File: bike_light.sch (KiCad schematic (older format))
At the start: 1 part

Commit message: Minor fixes, labels, etc
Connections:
- wire segments 70 -> 72
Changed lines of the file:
@@
 Sheet 1 18
 Title "Bike Light"
-Date "10 dec 2013"
+Date "11 dec 2013"
 Rev "1.0"
 Comp ""
@@
 F4 "~RESET" I L 7000 1800 60
 F5 "BATT_IN" I L 7000 1150 60
+F6 "PWR_GOOD" O R 7900 1650 60
+F7 "PWR_EN" I L 7000 1250 60
 $EndSheet
 $Sheet
@@
 Wire Wire Line
 	5200 5350 5500 5350
+Wire Wire Line
+	6900 1150 6900 1250
+Wire Wire Line
+	6900 1250 7000 1250
+Connection ~ 6900 1150
 $EndSCHEMATC

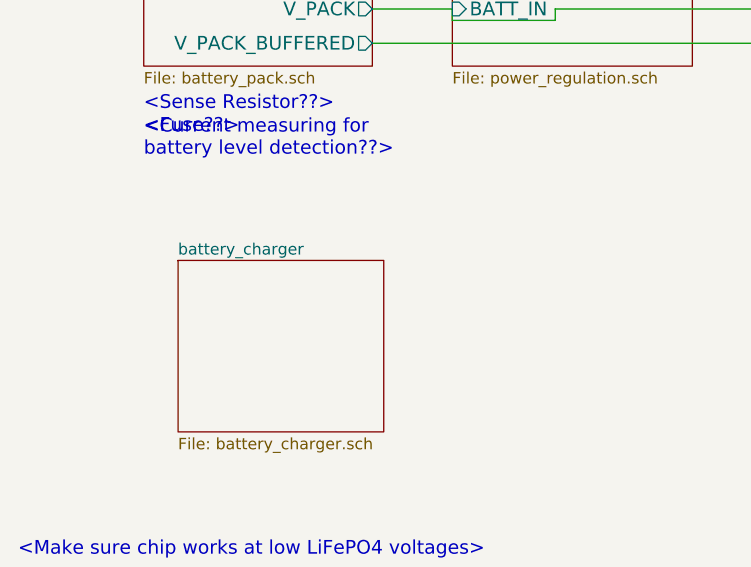
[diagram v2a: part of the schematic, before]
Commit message: started working on charging IC
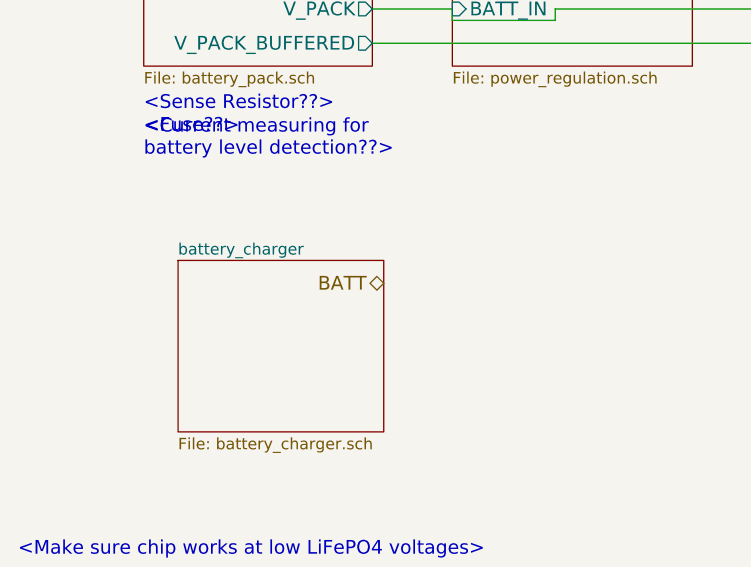
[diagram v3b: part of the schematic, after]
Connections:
- net labels added: BATT
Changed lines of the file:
@@
 Sheet 1 18
 Title "Bike Light"
-Date "11 dec 2013"
+Date "12 dec 2013"
 Rev "1.0"
 Comp ""
@@
 	6900 1250 7000 1250
 Connection ~ 6900 1150
+Text HLabel 2250 2350 0    60   BiDi ~ 0
+BATT
 $EndSCHEMATC

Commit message: uh. same as before? some glitch
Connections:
- wire segments 72 -> 71
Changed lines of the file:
@@
 Sheet 1 18
 Title "Bike Light"
-Date "12 dec 2013"
+Date "13 dec 2013"
 Rev "1.0"
 Comp ""
@@
 $EndSheet
 Wire Wire Line
-	2200 1150 2550 1150
-Wire Wire Line
 	2550 1150 2550 1200

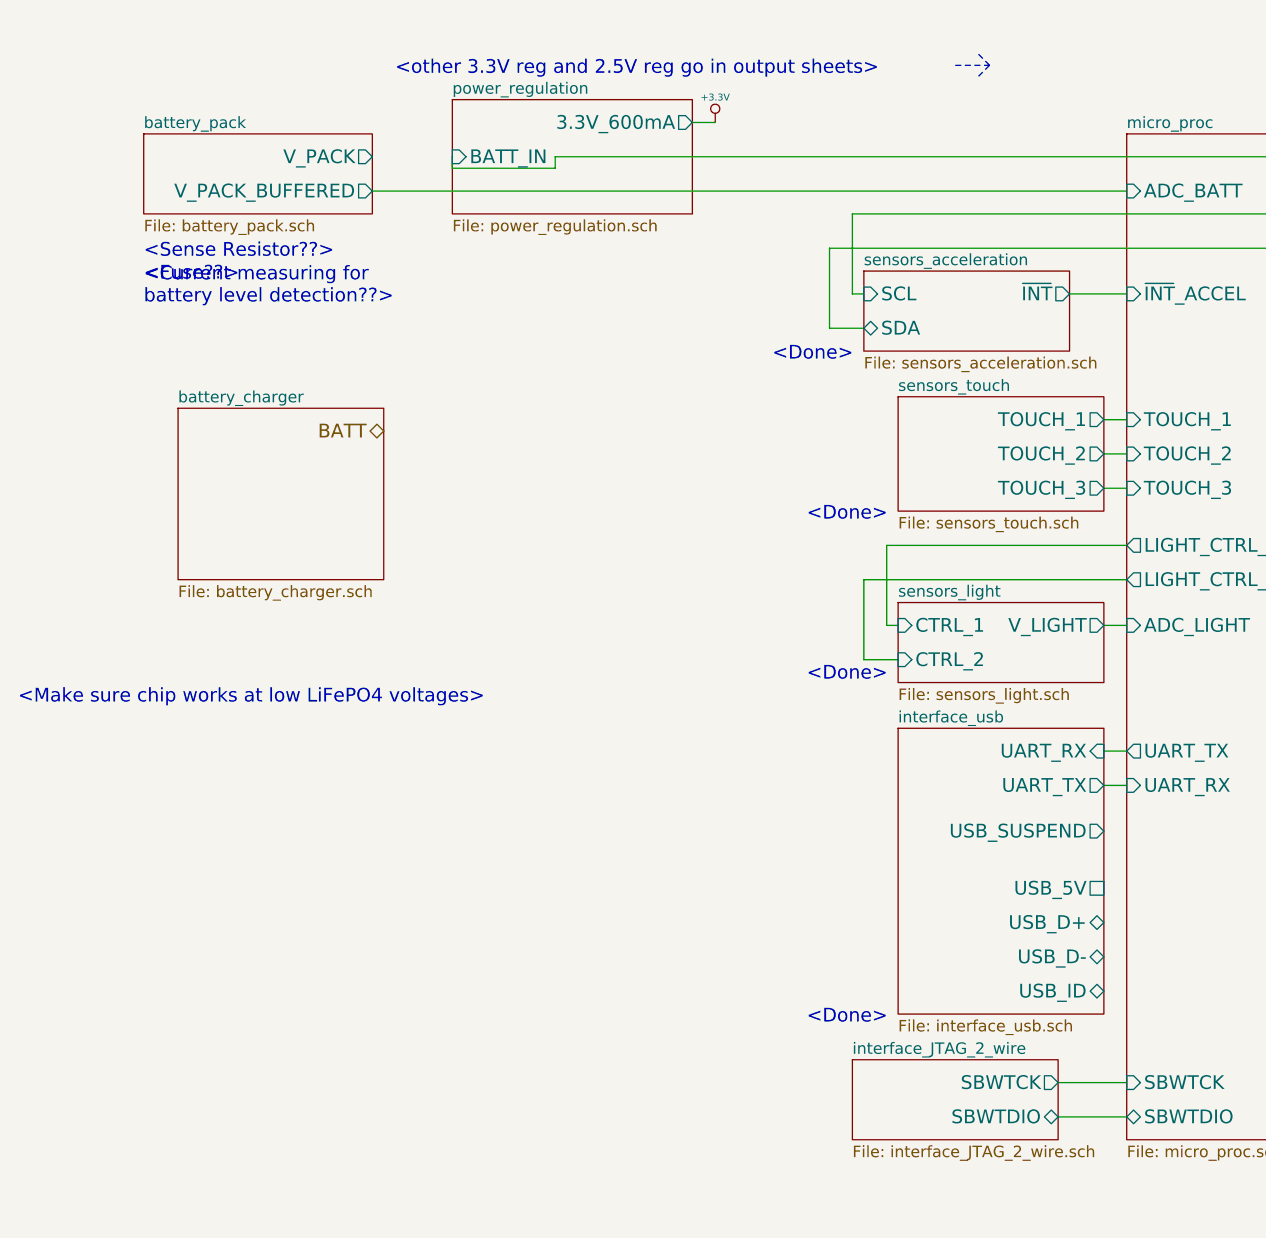
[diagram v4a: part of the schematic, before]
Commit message: finished schematic charger, need to part out caps and inductor
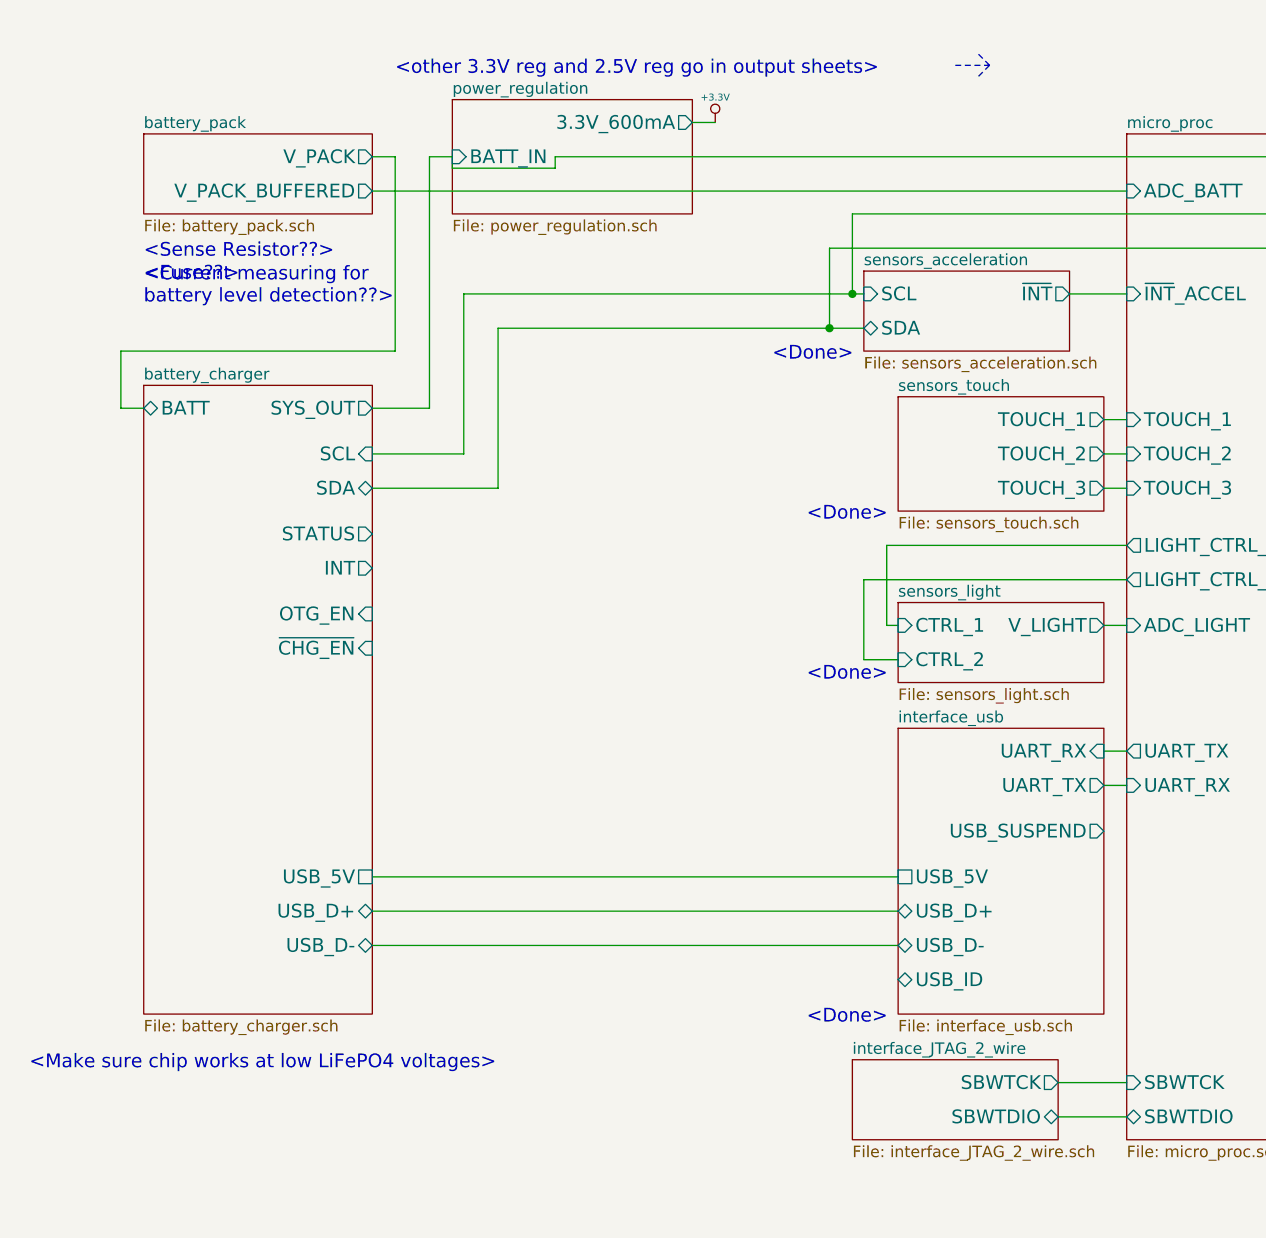
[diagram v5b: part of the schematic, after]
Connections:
- net labels removed: BATT
- wire segments 71 -> 86
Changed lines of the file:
@@
 Sheet 1 18
 Title "Bike Light"
-Date "13 dec 2013"
+Date "14 dec 2013"
 Rev "1.0"
 Comp ""
@@
 $EndSheet
 $Sheet
-S 4500 3650 900  1250
-U 5224C595
-F0 "interface_usb" 50
-F1 "interface_usb.sch" 50
-F2 "UART_RX" I R 5400 3750 60
-F3 "UART_TX" O R 5400 3900 60
-F4 "USB_SUSPEND" O R 5400 4100 60
-F5 "USB_5V" U R 5400 4350 60
-F6 "USB_D+" B R 5400 4500 60
-F7 "USB_D-" B R 5400 4650 60
-F8 "USB_ID" B R 5400 4800 60
-$EndSheet
-$Sheet
 S 7050 5800 900  200
 U 527B19B4
@@
 Text Notes 4100 4950 0    60   ~ 0
 <Done>
-Text Notes 650  3550 0    60   ~ 0
+Text Notes 700  5150 0    60   ~ 0
 <Make sure chip works at low LiFePO4 voltages>
-$Sheet
-S 1350 2250 900  750
-U 52929F4D
-F0 "battery_charger" 50
-F1 "battery_charger.sch" 50
-$EndSheet
 $Sheet
 S 7000 1050 900  850
@@
 	5400 2600 5500 2600
 Wire Wire Line
-	4300 1750 4350 1750
+	2600 1750 4350 1750
 Wire Wire Line
 	4300 1400 4300 1750
 Wire Wire Line
-	4350 1900 4200 1900
+	2750 1900 4350 1900
 Wire Wire Line
 	5250 1750 5500 1750
@@
 	6900 1250 7000 1250
 Connection ~ 6900 1150
-Text HLabel 2250 2350 0    60   BiDi ~ 0
-BATT
+$Sheet
+S 4500 3650 900  1250
+U 5224C595
+F0 "interface_usb" 50
+F1 "interface_usb.sch" 50
+F2 "UART_RX" I R 5400 3750 60
+F3 "UART_TX" O R 5400 3900 60
+F4 "USB_SUSPEND" O R 5400 4100 60
+F5 "USB_5V" U L 4500 4300 60
+F6 "USB_D+" B L 4500 4450 60
+F7 "USB_D-" B L 4500 4600 60
+F8 "USB_ID" B L 4500 4750 60
+$EndSheet
+Wire Wire Line
+	4500 4300 2200 4300
+Wire Wire Line
+	2200 4450 4500 4450
+Wire Wire Line
+	4500 4600 2200 4600
+Wire Wire Line
+	2200 1150 2300 1150
+Wire Wire Line
+	2300 1150 2300 2000
+Wire Wire Line
+	2300 2000 1100 2000
+Wire Wire Line
+	1100 2000 1100 2250
+Wire Wire Line
+	1100 2250 1200 2250
+Wire Wire Line
+	2200 2250 2450 2250
+Wire Wire Line
+	2450 2250 2450 1150
+Wire Wire Line
+	2450 1150 2550 1150
+Wire Wire Line
+	2200 2450 2600 2450
+Wire Wire Line
+	2600 2450 2600 1750
+Connection ~ 4300 1750
+Wire Wire Line
+	2200 2600 2750 2600
+Wire Wire Line
+	2750 2600 2750 1900
+Connection ~ 4200 1900
+$Sheet
+S 1200 2150 1000 2750
+U 52929F4D
+F0 "battery_charger" 50
+F1 "battery_charger.sch" 50
+F2 "USB_5V" U R 2200 4300 60
+F3 "USB_D+" B R 2200 4450 60
+F4 "USB_D-" B R 2200 4600 60
+F5 "STATUS" O R 2200 2800 60
+F6 "SCL" I R 2200 2450 60
+F7 "SDA" B R 2200 2600 60
+F8 "INT" O R 2200 2950 60
+F9 "OTG_EN" I R 2200 3150 60
+F10 "~CHG_EN" I R 2200 3300 60
+F11 "BATT" B L 1200 2250 60
+F12 "SYS_OUT" O R 2200 2250 60
+$EndSheet
 $EndSCHEMATC

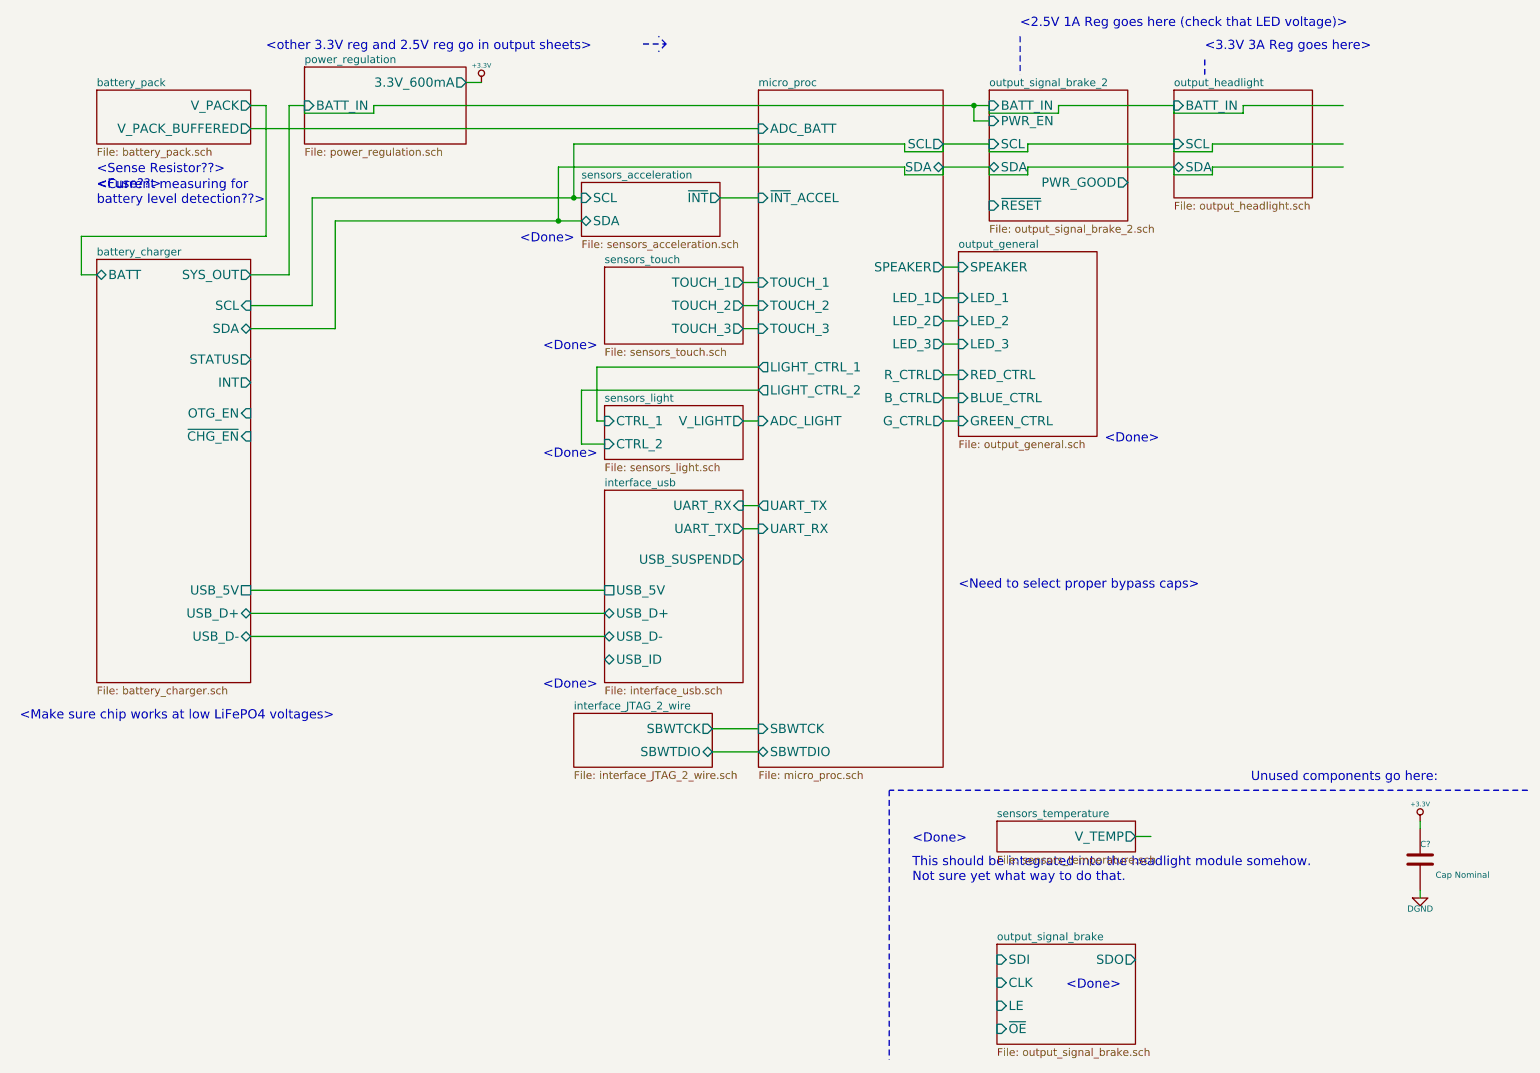
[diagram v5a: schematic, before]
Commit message: added pullups/downs as necessary, added test pts
also added interrupt conn to msp from charger, made led part for generic
indicators, added generic indicators to psu's
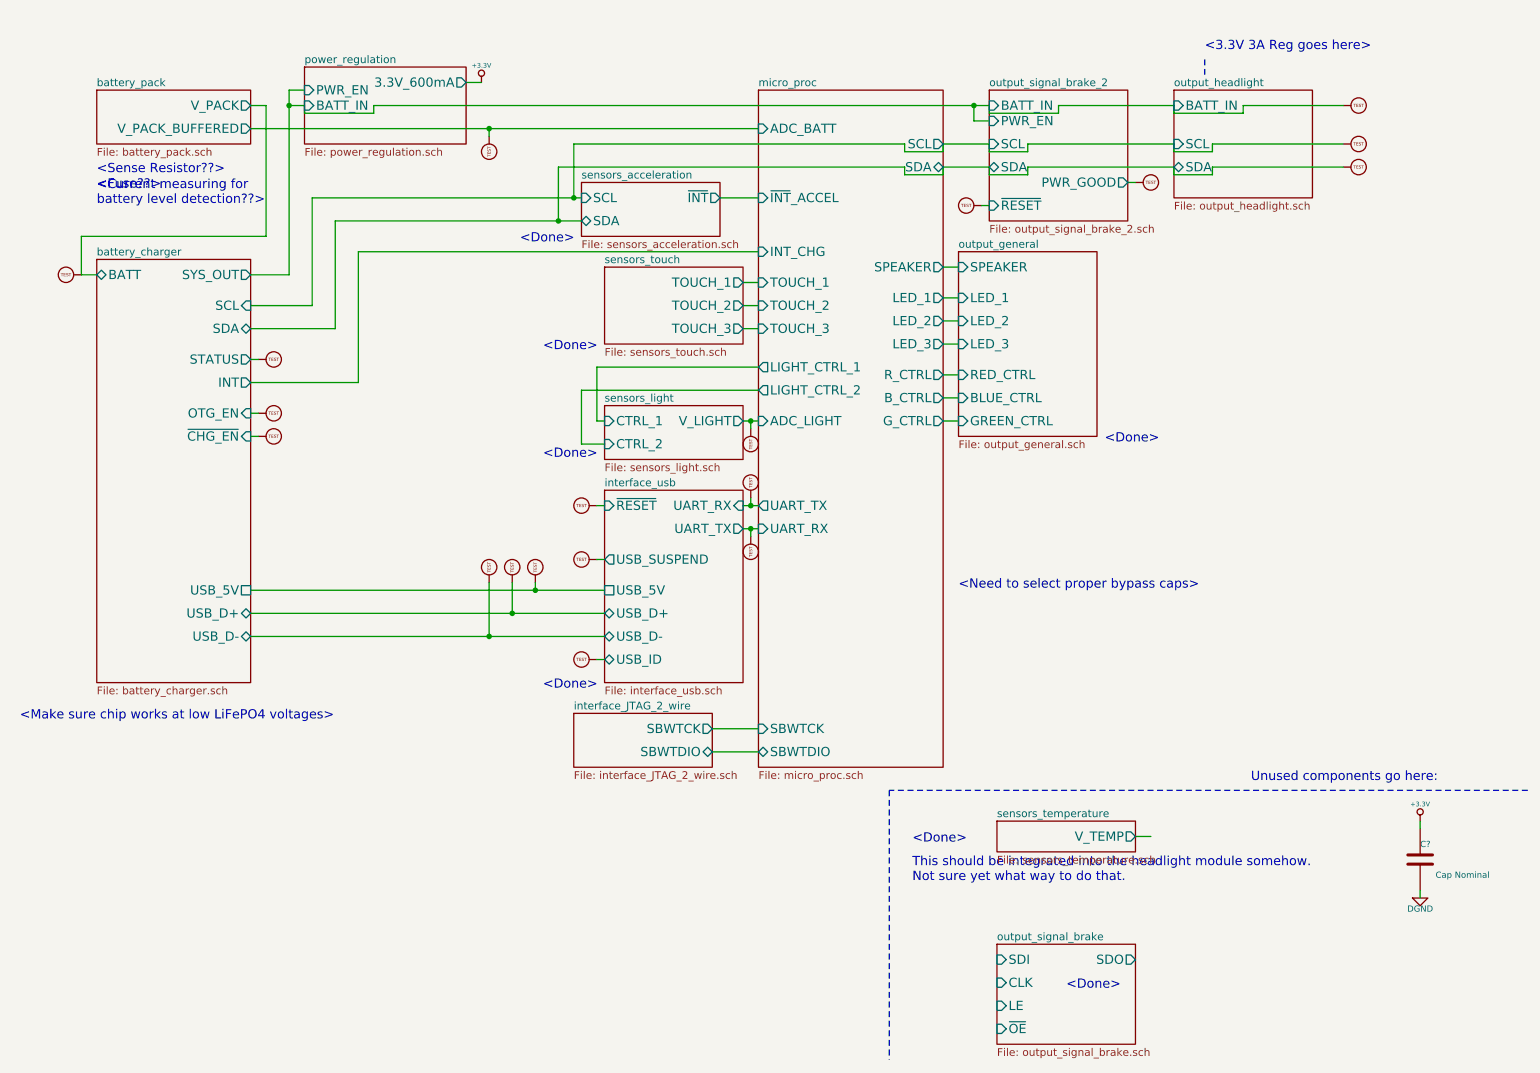
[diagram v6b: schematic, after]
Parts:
- added U? (x19): TEST_PT, ~, symbol TEST_PT
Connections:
- wire segments 86 -> 105
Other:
- note removed: "<2.5V 1A Reg goes here (check that LED voltage)>"
- note removed: "<other 3.3V reg and 2.5V reg go in output sheets>"
